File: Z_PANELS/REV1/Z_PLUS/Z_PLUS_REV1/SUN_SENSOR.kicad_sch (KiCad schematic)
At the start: 26 parts, among them IC1 LTC4316IDD#PBF, Q10 BSS138, Q11 BSS138, Q13 BSS138, Q14 BSS138, U2 OPT4001DTST

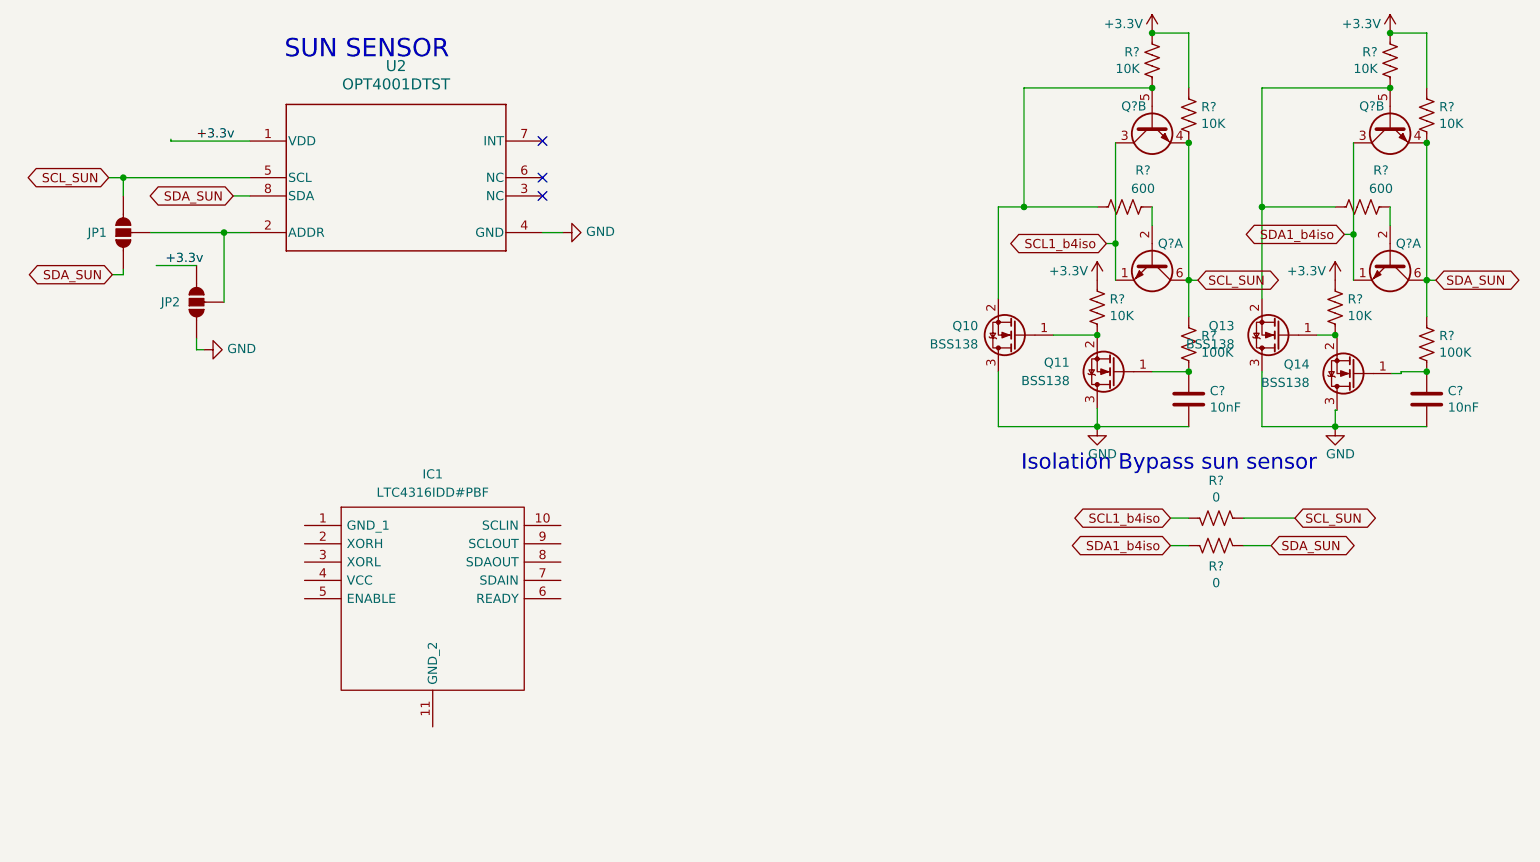
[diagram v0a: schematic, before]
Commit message: added dxf to z plus. incremental update
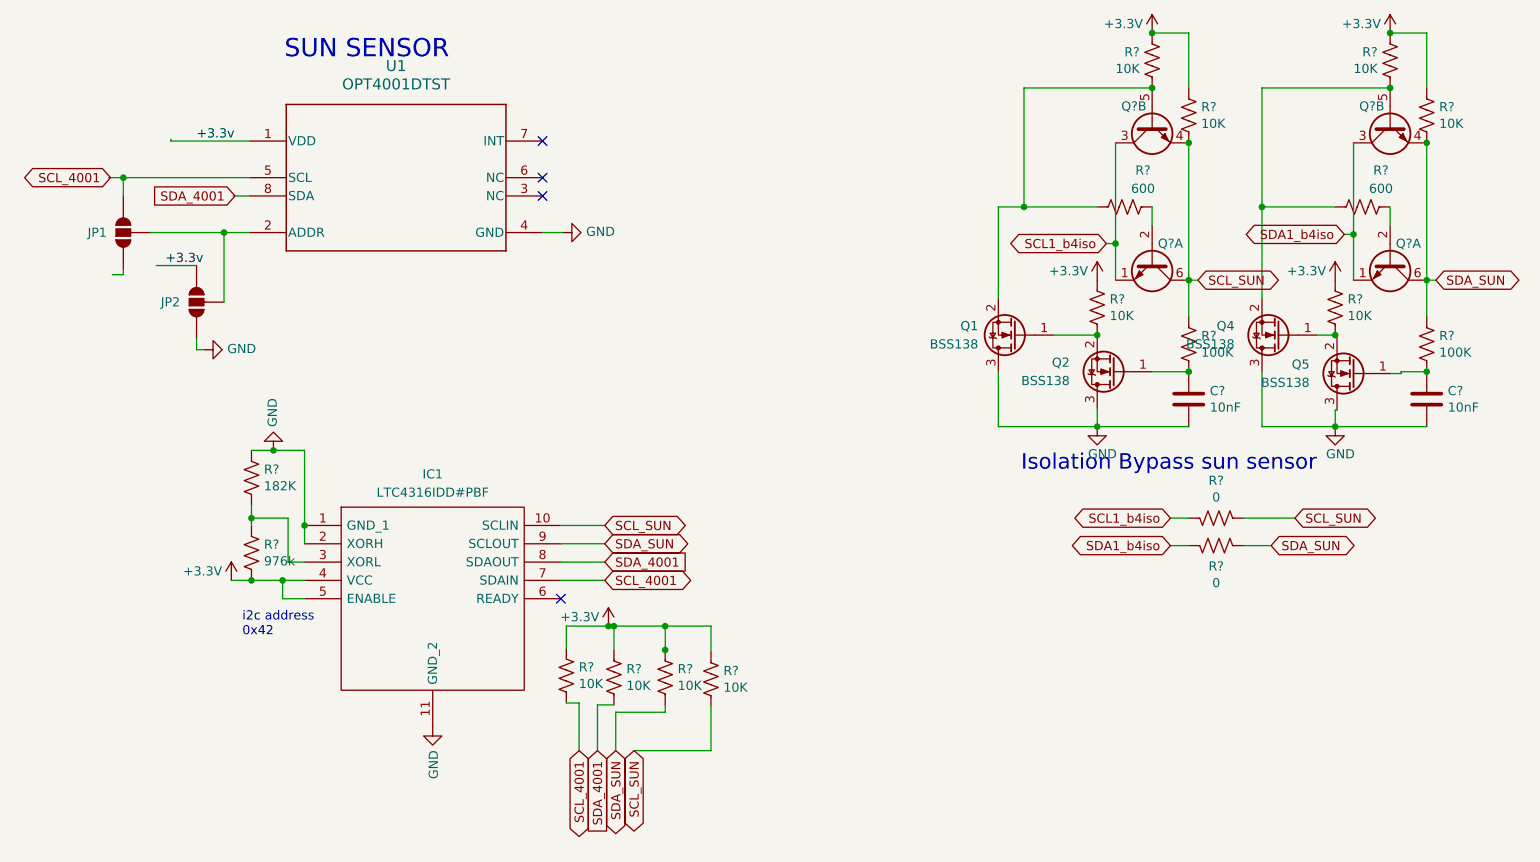
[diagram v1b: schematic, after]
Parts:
- added R? (x4): 10K, Resistor_SMD:R_0402_1005Metric, symbol Device:R_US
- added R?: 182K, Resistor_SMD:R_0402_1005Metric, symbol Device:R_US
- added R?: 976k, Resistor_SMD:R_0402_1005Metric, symbol Device:R_US
- renumbered Q10 to Q1, Q11 to Q2, Q13 to Q4, Q14 to Q5, U2 to U1
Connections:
- net +3.3V: now also IC1.4 (VCC), IC1.5 (ENABLE), R?.1, R?.2, R?.2, R?.2, R?.2
- net GND: now also IC1.1 (GND_1), IC1.11 (GND_2), IC1.2 (XORH), R?.2
- net SCL_SUN: now also IC1.10 (SCLIN), R?.1; no longer JP1.3 (B), U1.5 (SCL)
- net SDA_SUN: now also IC1.9 (SCLOUT), R?.1; no longer JP1.1 (A), U1.8 (SDA)
- net at IC1.3 (XORL): now also R?.1, R?.2
- net SCL_4001: now reaches IC1.7 (SDAIN)
- net SCL_4001: now also JP1.3 (B), U1.5 (SCL), R?.1
- net SDA_4001: now reaches IC1.8 (SDAOUT)
- net SDA_4001: now also U1.8 (SDA), R?.1
- no-connect marks 3 -> 4
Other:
- note added: "i2c address 0x42"

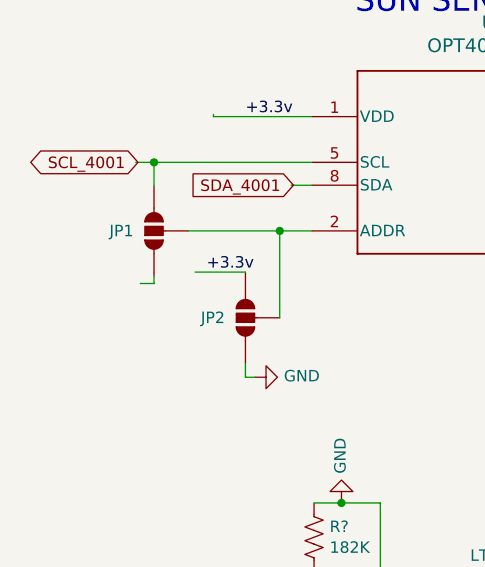
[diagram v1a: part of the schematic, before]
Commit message: initial routing z plus
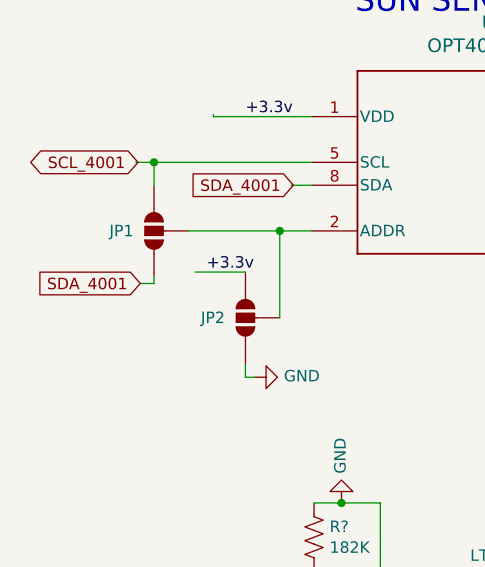
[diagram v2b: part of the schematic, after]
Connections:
- net SDA_4001: now also JP1.1 (A)
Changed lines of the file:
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@@
+    )
+  )
+  (global_label "SDA_4001" (shape input) (at 46.482 82.804 180) (fields_autoplaced)
+    (effects (font (size 1.27 1.27)) (justify right))
+    (property "Intersheetrefs" "${INTERSHEET_REFS}" (at 34.1231 82.804 0)
+      (effects (font (size 1.27 1.27)) (justify right) hide)
     )
   )
